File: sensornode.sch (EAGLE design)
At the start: 72 parts, among them IC1 CP2104, Q1 mmbt2222, Q2 mmbt2222, Q3 DMG3415U, SW2 KMR2, U1 TSL2591, U2 AP2112-3.3, U3 MCP73831T-2ACI/OT, U4 BMEx80, X2 ESP32_WROOM32_SKINNY, X4 20329

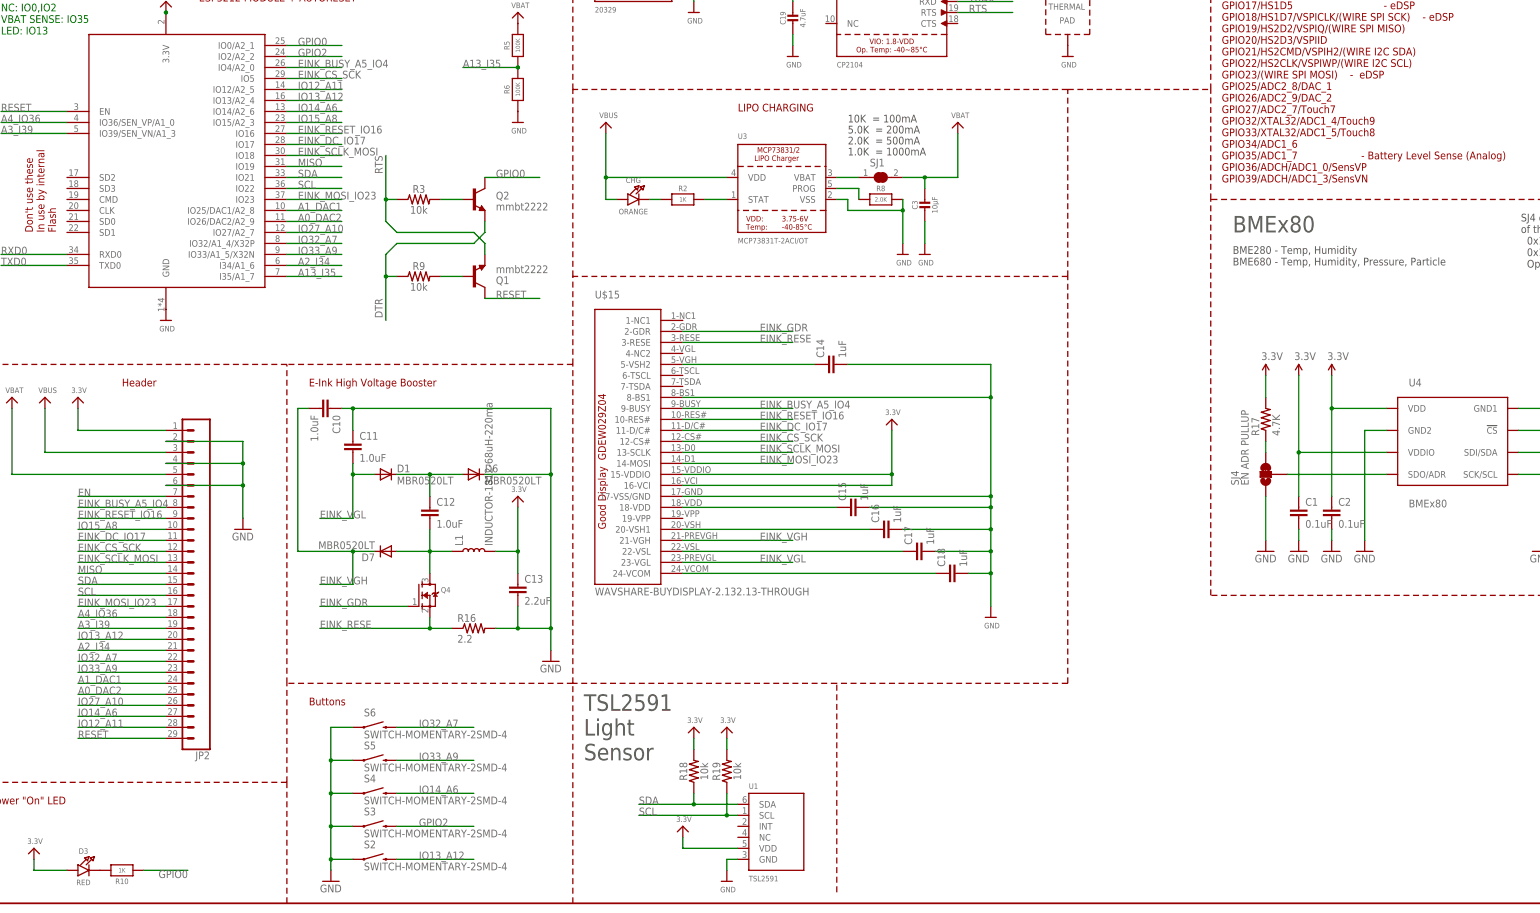
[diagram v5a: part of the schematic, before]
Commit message: Adding SD Card
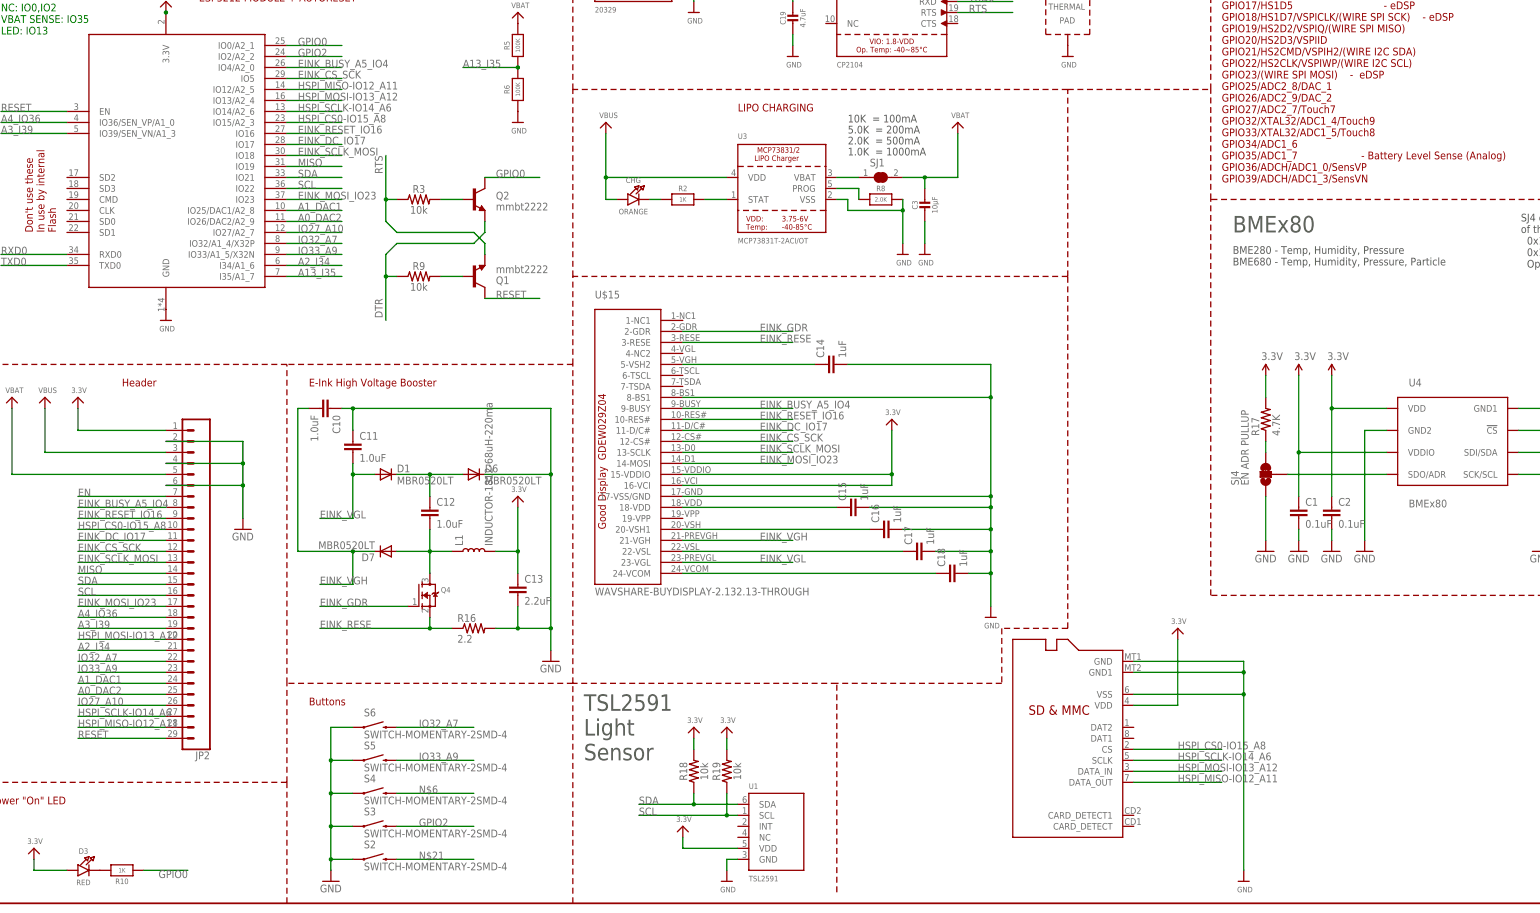
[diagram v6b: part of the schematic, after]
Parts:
- added U$17: MICROSD, adafruit:MICROSD
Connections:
- removed net IO12_A11: JP2.28, X2.IO12/A2_5
- removed net IO13_A12: JP2.20, S2.2, X2.IO13/A2_4
- removed net IO14_A6: JP2.27, S4.2, X2.IO14/A2_6
- removed net IO15_A8: JP2.10, X2.IO15/A2_3
- new net HSPI_CS0-IO15_A8: JP2.10, U$17.CS, X2.IO15/A2_3
- new net HSPI_MISO-IO12_A11: JP2.28, U$17.DATA_OUT, X2.IO12/A2_5
- new net HSPI_MOSI-IO13_A12: JP2.20, U$17.DATA_IN, X2.IO13/A2_4
- new net HSPI_SCLK-IO14_A6: JP2.27, U$17.SCLK, X2.IO14/A2_6
- new net N$21: S2.2
- new net N$6: S4.2
- net 3.3V: now also U$17.VDD
- net GND: now also U$17.GND, U$17.GND1, U$17.VSS
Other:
- note added: "BME280 - Temp, Humidity, Pressure BME680 - Temp, Humidity, Pressure, Particle"
- note removed: "BME280 - Temp, Humidity BME680 - Temp, Humidity, Pressure, Particle"
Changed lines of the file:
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@@
 <part name="U$47" library="microbuilder" deviceset="GND" device=""/>
 <part name="U$18" library="microbuilder" deviceset="VBUS" device=""/>
+<part name="U$17" library="adafruit" deviceset="MICROSD" device=""/>
+<part name="U$31" library="microbuilder" deviceset="GND" device=""/>
+<part name="U$45" library="microbuilder" deviceset="3.3V" device=""/>
 </parts>
 <sheets>
@@
 <wire x1="71.12" y1="50.8" x2="71.12" y2="124.46" width="0.1524" layer="94" style="shortdash"/>
 <wire x1="251.46" y1="187.96" x2="284.48" y2="187.96" width="0.1524" layer="94" style="shortdash"/>
-<wire x1="251.46" y1="50.8" x2="251.46" y2="144.78" width="0.1524" layer="94" style="shortdash"/>
+<wire x1="251.46" y1="63.5" x2="251.46" y2="144.78" width="0.1524" layer="94" style="shortdash"/>
 <wire x1="251.46" y1="144.78" x2="251.46" y2="187.96" width="0.1524" layer="94" style="shortdash"/>
-<wire x1="251.46" y1="50.8" x2="198.12" y2="50.8" width="0.1524" layer="94" style="shortdash"/>
+<wire x1="251.46" y1="63.5" x2="236.22" y2="63.5" width="0.1524" layer="94" style="shortdash"/>
+<wire x1="236.22" y1="63.5" x2="236.22" y2="50.8" width="0.1524" layer="94" style="shortdash"/>
+<wire x1="236.22" y1="50.8" x2="198.12" y2="50.8" width="0.1524" layer="94" style="shortdash"/>
 <text x="50.8" y="208.28" size="1.778" layer="94">ESP3212 MODULE + AUTORESET</text>
 <text x="5.08" y="200.66" size="1.778" layer="91">NC: IO0,IO2
@@
   0x1110111
   Open for SPI 3-wire mode</text>
-<text x="289.56" y="147.32" size="1.778" layer="97">BME280 - Temp, Humidity
+<text x="289.56" y="147.32" size="1.778" layer="97">BME280 - Temp, Humidity, Pressure
 BME680 - Temp, Humidity, Pressure, Particle</text>
 <wire x1="284.48" y1="71.12" x2="284.48" y2="162.56" width="0.1524" layer="94" style="shortdash"/>
@@
 <instance part="U$47" gate="G$1" x="177.8" y="226.06"/>
 <instance part="U$18" gate="G$1" x="167.64" y="259.08"/>
+<instance part="U$17" gate="G$1" x="248.92" y="35.56" rot="R180"/>
+<instance part="U$31" gate="G$1" x="292.1" y="5.08"/>
+<instance part="U$45" gate="G$1" x="276.86" y="63.5"/>
 </instances>
 <busses>
@@
 <wire x1="185.42" y1="231.14" x2="185.42" y2="228.6" width="0.1524" layer="91"/>
 </segment>
+<segment>
+<pinref part="U$17" gate="G$1" pin="GND"/>
+<wire x1="266.7" y1="55.88" x2="292.1" y2="55.88" width="0.1524" layer="91"/>
+<wire x1="292.1" y1="55.88" x2="292.1" y2="53.34" width="0.1524" layer="91"/>
+<pinref part="U$31" gate="G$1" pin="GND"/>
+<pinref part="U$17" gate="G$1" pin="GND1"/>
+<wire x1="292.1" y1="53.34" x2="292.1" y2="48.26" width="0.1524" layer="91"/>
+<wire x1="292.1" y1="48.26" x2="292.1" y2="7.62" width="0.1524" layer="91"/>
+<wire x1="266.7" y1="53.34" x2="292.1" y2="53.34" width="0.1524" layer="91"/>
+<junction x="292.1" y="53.34"/>
+<pinref part="U$17" gate="G$1" pin="VSS"/>
+<wire x1="266.7" y1="48.26" x2="292.1" y2="48.26" width="0.1524" layer="91"/>
+<junction x="292.1" y="48.26"/>
+</segment>
 </net>
 <net name="TXLED" class="0">
@@
 <wire x1="193.04" y1="246.38" x2="195.58" y2="246.38" width="0.1524" layer="91"/>
 </segment>
+<segment>
+<pinref part="U$17" gate="G$1" pin="VDD"/>
+<pinref part="U$45" gate="G$1" pin="3.3V"/>
+<wire x1="266.7" y1="45.72" x2="276.86" y2="45.72" width="0.1524" layer="91"/>
+<wire x1="276.86" y1="45.72" x2="276.86" y2="60.96" width="0.1524" layer="91"/>
+</segment>
 </net>
 <net name="RESET" class="0">
@@
 </segment>
 </net>
-<net name="IO13_A12" class="0">
+<net name="HSPI_MOSI-IO13_A12" class="0">
 <segment>
 <wire x1="71.12" y1="185.42" x2="83.82" y2="185.42" width="0.1524" layer="91"/>
@@
 </segment>
 <segment>
-<wire x1="96.52" y1="10.16" x2="114.3" y2="10.16" width="0.1524" layer="91"/>
-<label x="101.6" y="10.16" size="1.778" layer="95"/>
-<pinref part="S2" gate="G$1" pin="2"/>
+<pinref part="U$17" gate="G$1" pin="DATA_IN"/>
+<wire x1="266.7" y1="30.48" x2="287.02" y2="30.48" width="0.1524" layer="91"/>
+<label x="276.86" y="30.48" size="1.778" layer="95"/>
 </segment>
 </net>
@@
 </segment>
 </net>
-<net name="IO12_A11" class="0">
+<net name="HSPI_MISO-IO12_A11" class="0">
 <segment>
 <wire x1="71.12" y1="187.96" x2="83.82" y2="187.96" width="0.1524" layer="91"/>
@@
 <label x="22.86" y="40.64" size="1.778" layer="95"/>
 </segment>
-</net>
-<net name="IO15_A8" class="0">
+<segment>
+<pinref part="U$17" gate="G$1" pin="DATA_OUT"/>
+<wire x1="266.7" y1="27.94" x2="287.02" y2="27.94" width="0.1524" layer="91"/>
+<label x="276.86" y="27.94" size="1.778" layer="95"/>
+</segment>
+</net>
+<net name="HSPI_CS0-IO15_A8" class="0">
 <segment>
 <wire x1="71.12" y1="180.34" x2="83.82" y2="180.34" width="0.1524" layer="91"/>
@@
 <wire x1="43.18" y1="86.36" x2="22.86" y2="86.36" width="0.1524" layer="91"/>
 <label x="22.86" y="86.36" size="1.778" layer="95"/>
+</segment>
+<segment>
+<pinref part="U$17" gate="G$1" pin="CS"/>
+<wire x1="266.7" y1="35.56" x2="287.02" y2="35.56" width="0.1524" layer="91"/>
+<label x="276.86" y="35.56" size="1.778" layer="95"/>
 </segment>
 </net>
@@
 </segment>
 </net>
-<net name="IO14_A6" class="0">
+<net name="HSPI_SCLK-IO14_A6" class="0">
 <segment>
 <wire x1="71.12" y1="182.88" x2="83.82" y2="182.88" width="0.1524" layer="91"/>
@@
 </segment>
 <segment>
-<pinref part="S4" gate="G$1" pin="2"/>
-<wire x1="96.52" y1="25.4" x2="114.3" y2="25.4" width="0.1524" layer="91"/>
-<label x="101.6" y="25.4" size="1.778" layer="95"/>
+<pinref part="U$17" gate="G$1" pin="SCLK"/>
+<wire x1="266.7" y1="33.02" x2="287.02" y2="33.02" width="0.1524" layer="91"/>
+<label x="276.86" y="33.02" size="1.778" layer="95"/>
 </segment>
 </net>
@@
 </segment>
 </net>
+<net name="N$6" class="0">
+<segment>
+<pinref part="S4" gate="G$1" pin="2"/>
+<wire x1="96.52" y1="25.4" x2="114.3" y2="25.4" width="0.1524" layer="91"/>
+<label x="101.6" y="25.4" size="1.778" layer="95"/>
+</segment>
+</net>
+<net name="N$21" class="0">
+<segment>
+<pinref part="S2" gate="G$1" pin="2"/>
+<wire x1="96.52" y1="10.16" x2="114.3" y2="10.16" width="0.1524" layer="91"/>
+<label x="101.6" y="10.16" size="1.778" layer="95"/>
+</segment>
+</net>

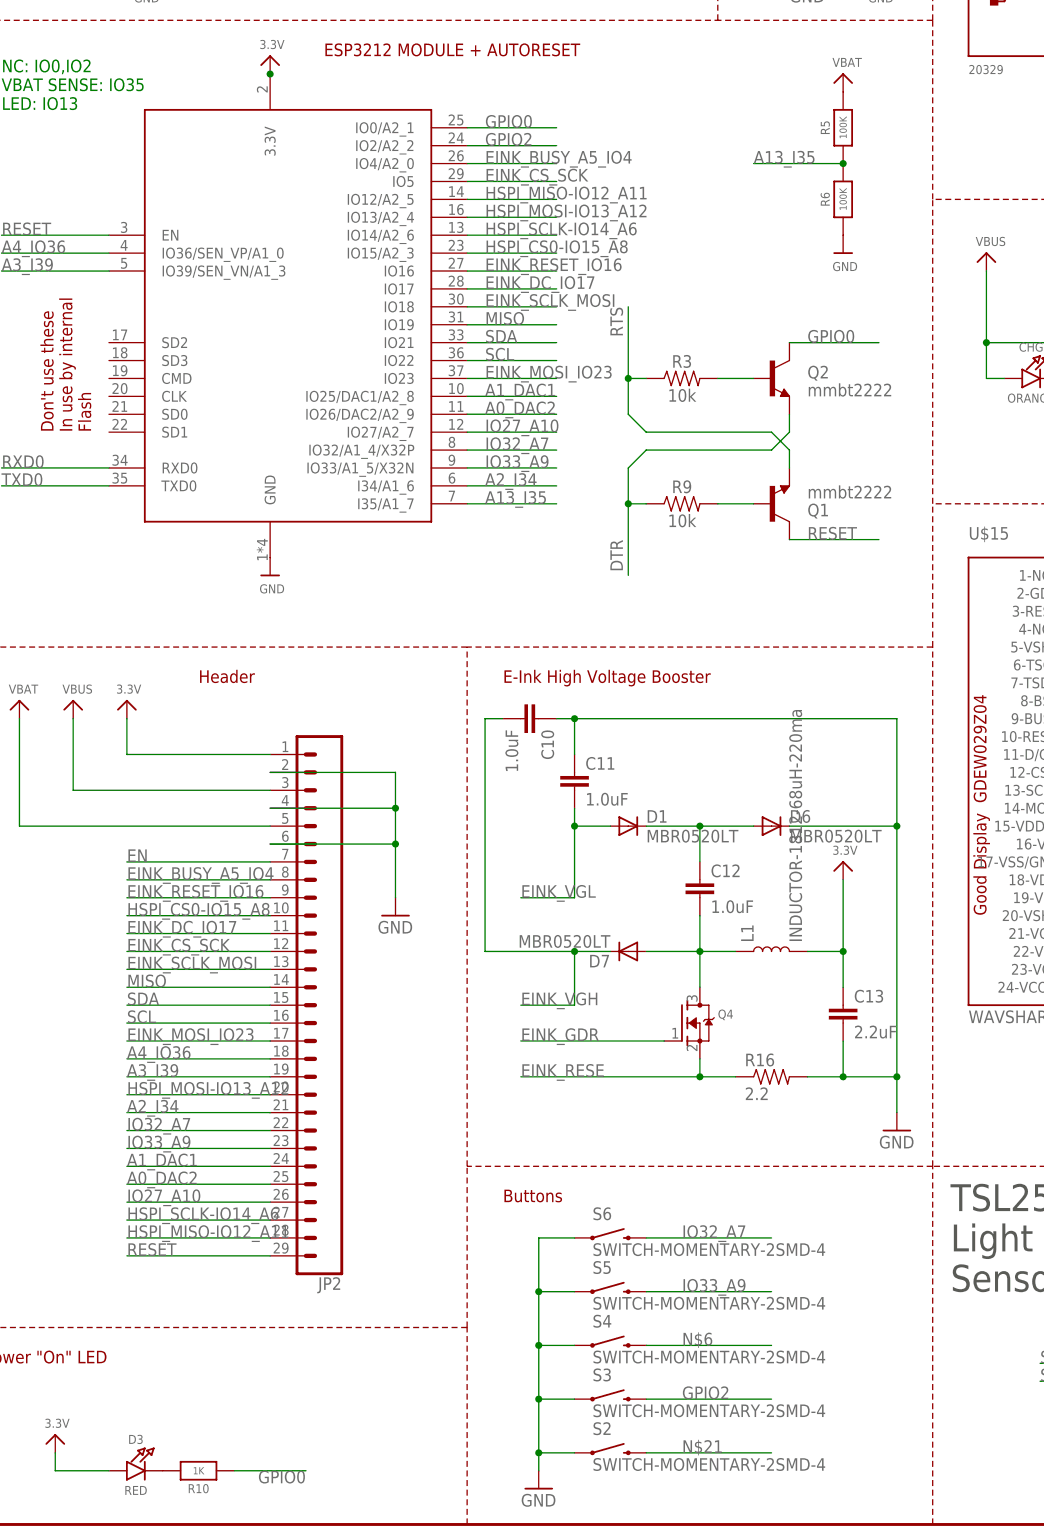
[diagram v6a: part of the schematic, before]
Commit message: Redoing the buttons
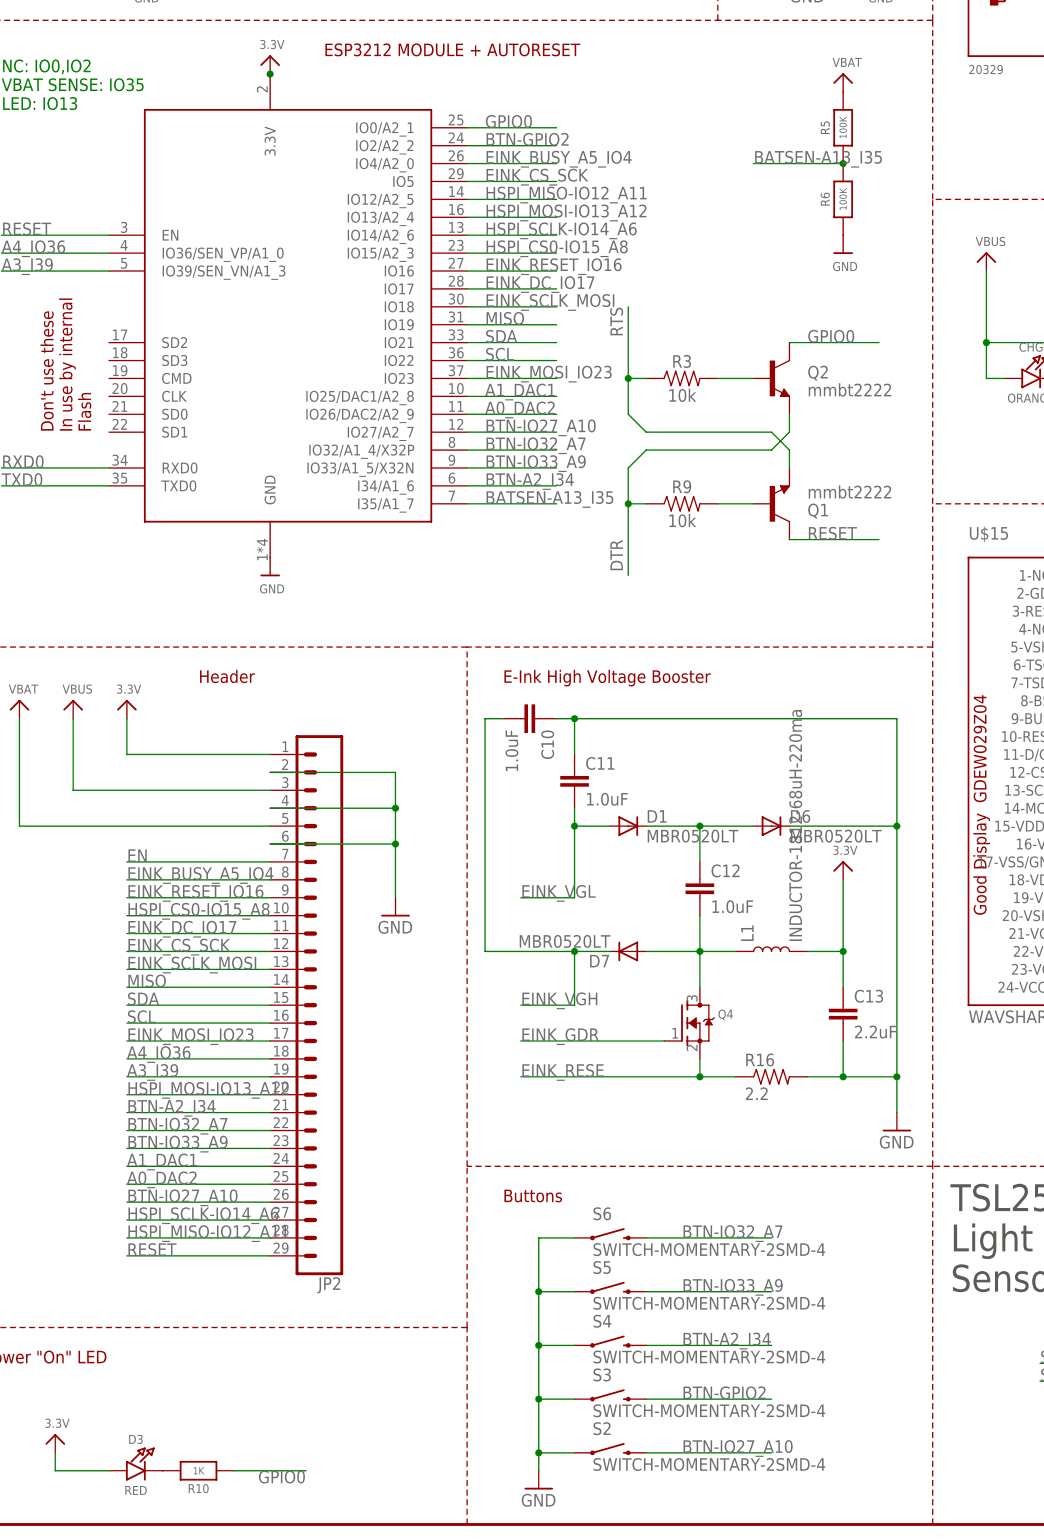
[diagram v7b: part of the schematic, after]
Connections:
- net A13_I35 renamed BATSEN-A13_I35
- net GPIO2 renamed BTN-GPIO2
- net IO32_A7 renamed BTN-IO32_A7
- net IO33_A9 renamed BTN-IO33_A9
- removed net A2_I34: JP2.21, X2.I34/A1_6
- removed net IO27_A10: JP2.26, X2.IO27/A2_7
- removed net N$21: S2.2
- removed net N$6: S4.2
- new net BTN-A2_I34: JP2.21, S4.2, X2.I34/A1_6
- new net BTN-IO27_A10: JP2.26, S2.2, X2.IO27/A2_7
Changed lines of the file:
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@@
 </segment>
 </net>
-<net name="GPIO2" class="0">
+<net name="BTN-GPIO2" class="0">
 <segment>
 <wire x1="71.12" y1="195.58" x2="83.82" y2="195.58" width="0.1524" layer="91"/>
@@
 </segment>
 </net>
-<net name="IO33_A9" class="0">
+<net name="BTN-IO33_A9" class="0">
 <segment>
 <wire x1="71.12" y1="149.86" x2="83.82" y2="149.86" width="0.1524" layer="91"/>
@@
 </segment>
 </net>
-<net name="IO32_A7" class="0">
+<net name="BTN-IO32_A7" class="0">
 <segment>
 <wire x1="71.12" y1="152.4" x2="83.82" y2="152.4" width="0.1524" layer="91"/>
@@
 </segment>
 </net>
-<net name="IO27_A10" class="0">
+<net name="BTN-IO27_A10" class="0">
 <segment>
 <wire x1="71.12" y1="154.94" x2="83.82" y2="154.94" width="0.1524" layer="91"/>
@@
 <label x="22.86" y="45.72" size="1.778" layer="95"/>
 </segment>
+<segment>
+<pinref part="S2" gate="G$1" pin="2"/>
+<wire x1="96.52" y1="10.16" x2="114.3" y2="10.16" width="0.1524" layer="91"/>
+<label x="101.6" y="10.16" size="1.778" layer="95"/>
+</segment>
 </net>
 <net name="MISO" class="0">
@@
 </segment>
 </net>
-<net name="A2_I34" class="0">
+<net name="BTN-A2_I34" class="0">
 <segment>
 <wire x1="71.12" y1="147.32" x2="83.82" y2="147.32" width="0.1524" layer="91"/>
@@
 <label x="22.86" y="58.42" size="1.778" layer="95"/>
 </segment>
-</net>
-<net name="A13_I35" class="0">
+<segment>
+<pinref part="S4" gate="G$1" pin="2"/>
+<wire x1="96.52" y1="25.4" x2="114.3" y2="25.4" width="0.1524" layer="91"/>
+<label x="101.6" y="25.4" size="1.778" layer="95"/>
+</segment>
+</net>
+<net name="BATSEN-A13_I35" class="0">
 <segment>
 <wire x1="71.12" y1="144.78" x2="83.82" y2="144.78" width="0.1524" layer="91"/>
@@
 </segment>
 </net>
-<net name="N$6" class="0">
-<segment>
-<pinref part="S4" gate="G$1" pin="2"/>
-<wire x1="96.52" y1="25.4" x2="114.3" y2="25.4" width="0.1524" layer="91"/>
-<label x="101.6" y="25.4" size="1.778" layer="95"/>
-</segment>
-</net>
-<net name="N$21" class="0">
-<segment>
-<pinref part="S2" gate="G$1" pin="2"/>
-<wire x1="96.52" y1="10.16" x2="114.3" y2="10.16" width="0.1524" layer="91"/>
-<label x="101.6" y="10.16" size="1.778" layer="95"/>
-</segment>
-</net>
